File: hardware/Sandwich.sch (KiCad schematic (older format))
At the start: 20 parts, among them P1 CONN_01X20, P2 CONN_01X06, P3 VGA_OUT, Q1 PZT2222A, U1 P8X32A-D40, U2 24C512, Y1 5MHz

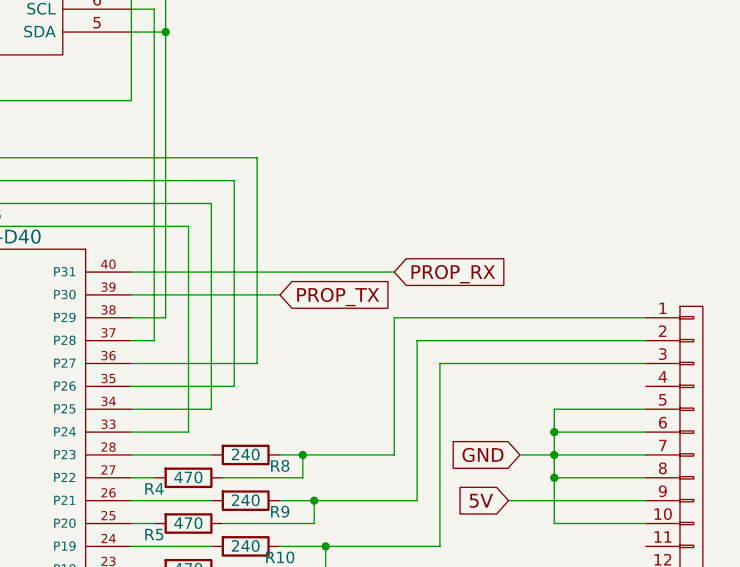
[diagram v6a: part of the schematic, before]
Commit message: TX/RX pins were switched over. Regenerated PCB and everything else.
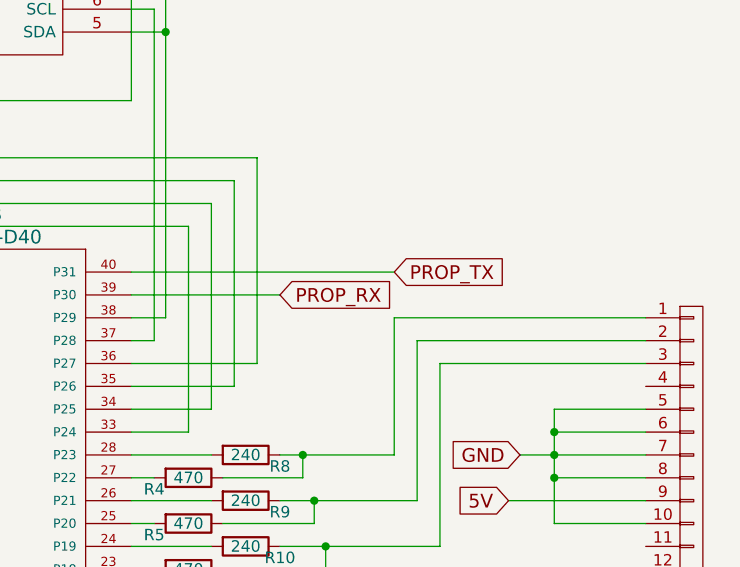
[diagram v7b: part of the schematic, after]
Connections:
- net PROP_RX: now also U1.39 (P30); no longer U1.40 (P31)
- net PROP_TX: now also U1.40 (P31); no longer U1.39 (P30)
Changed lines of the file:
@@
 Connection ~ 4950 2850
 Text GLabel 6800 3600 2    60   Input ~ 0
+PROP_TX
+Text GLabel 6300 3700 2    60   Input ~ 0
 PROP_RX
-Text GLabel 6300 3700 2    60   Input ~ 0
-PROP_TX
 Wire Wire Line
 	4200 5300 4350 5300

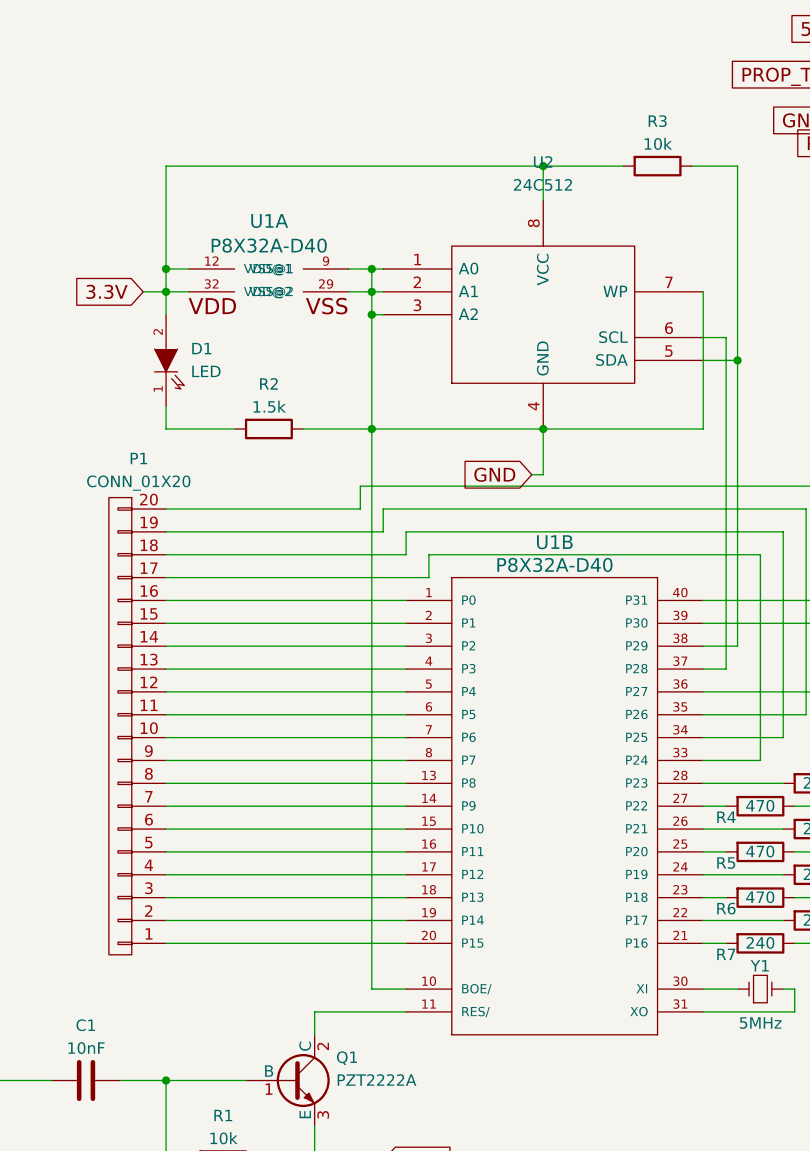
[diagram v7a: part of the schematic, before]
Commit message: Added a cap.
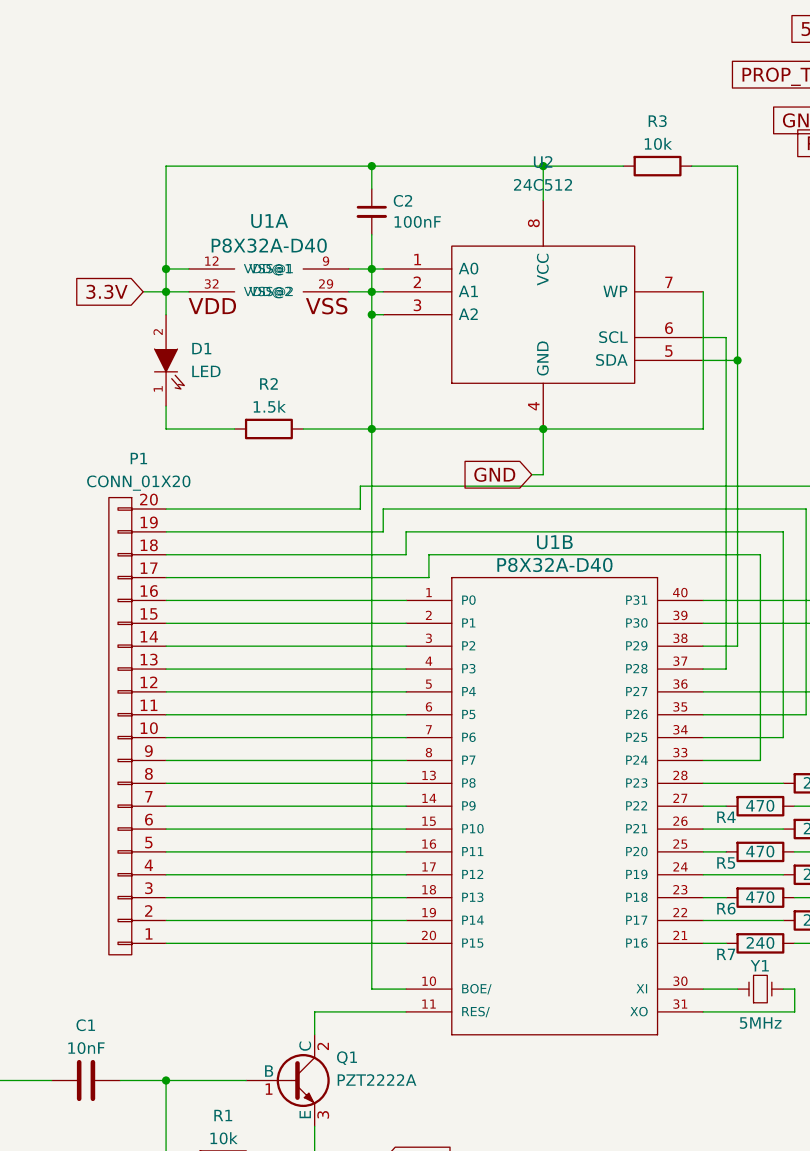
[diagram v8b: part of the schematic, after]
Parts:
- added C2: 100nF, symbol C_Small
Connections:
- net 3.3V: now also C2.1
- net GND: now also C2.2
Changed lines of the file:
@@
 	3900 2850 5650 2850
 Wire Wire Line
-	4200 2150 4200 5300
+	4200 2000 4200 5300
 Connection ~ 4200 2250
 Connection ~ 4200 2150
@@
 Wire Wire Line
 	6200 4000 5650 4000
+$Comp
+L C_Small C2
+U 1 1 56D1DFFB
+P 4200 1900
+F 0 "C2" H 4292 1946 50  0000 L CNN
+F 1 "100nF" H 4292 1854 50  0000 L CNN
+F 2 "" H 4200 1900 50  0000 C CNN
+F 3 "" H 4200 1900 50  0000 C CNN
+	1    4200 1900
+	1    0    0    -1
+$EndComp
+Wire Wire Line
+	4200 1800 4200 1700
+Connection ~ 4200 1700
 $EndSCHEMATC
